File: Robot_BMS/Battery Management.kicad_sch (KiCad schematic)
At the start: 13 parts, among them IC1 BQ76922RSNR

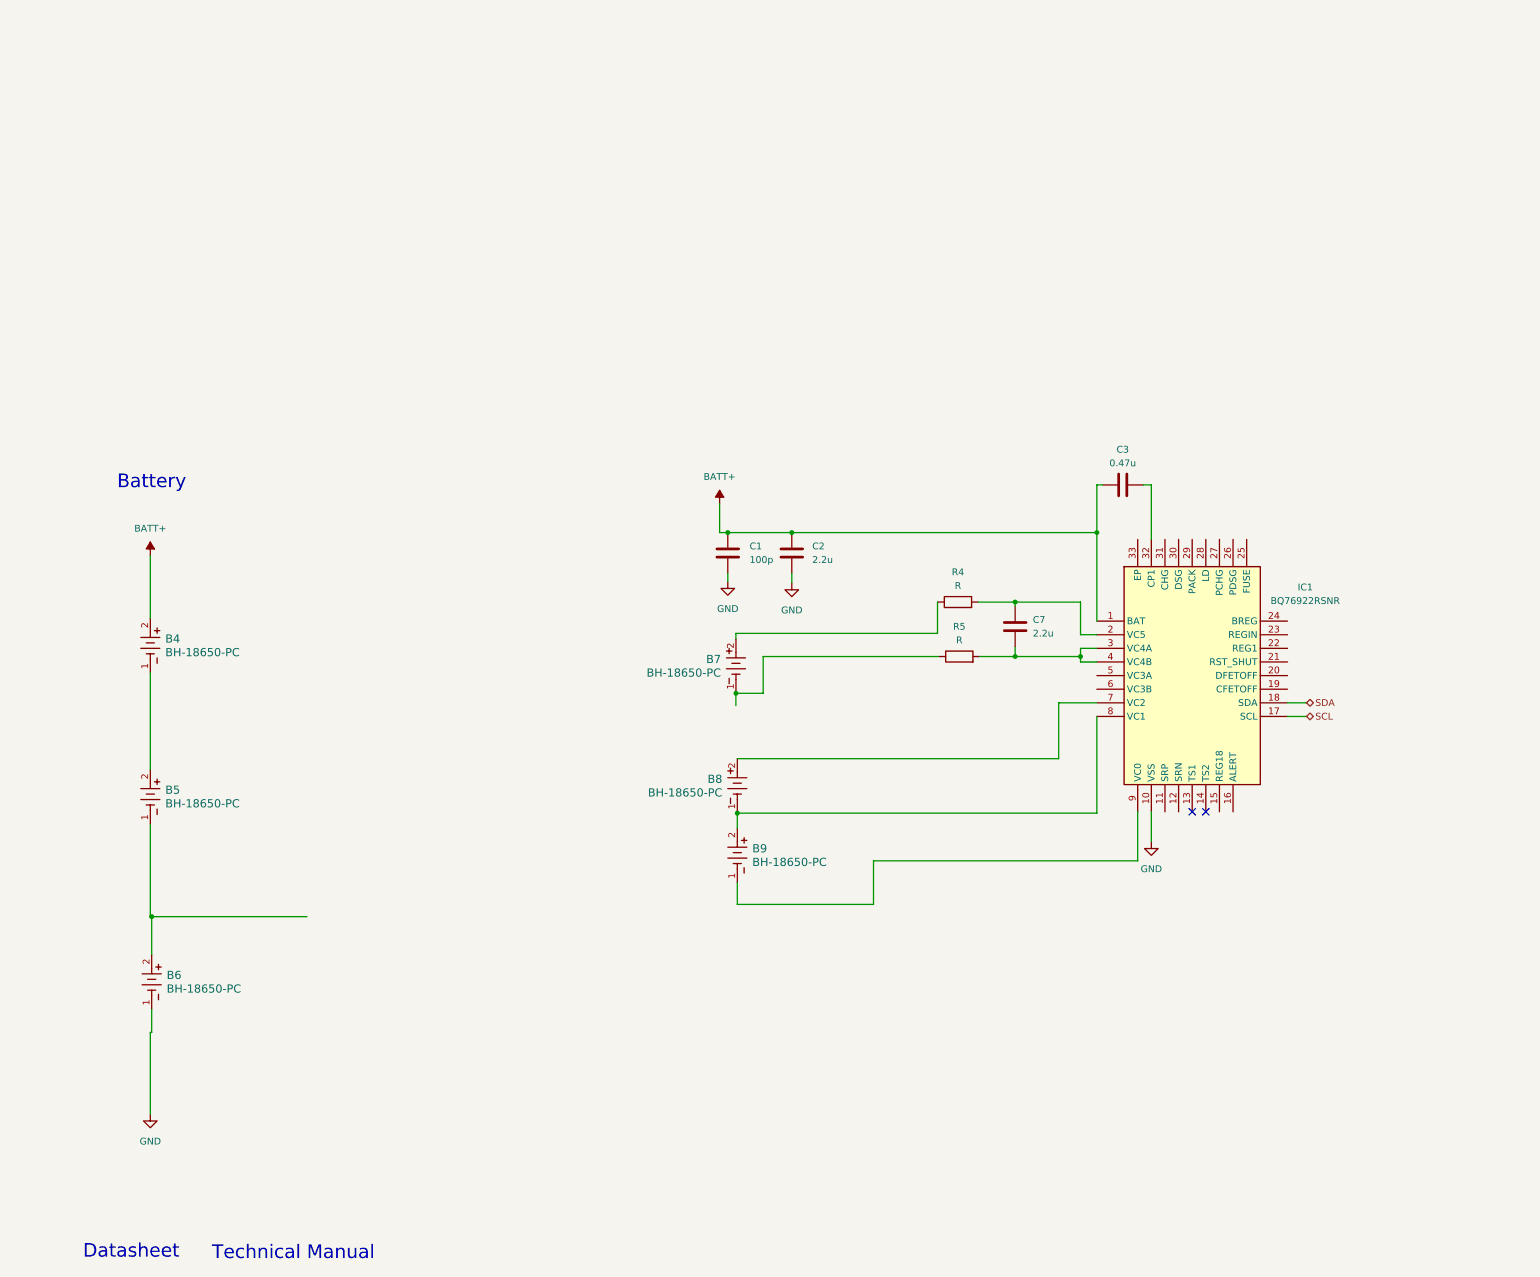
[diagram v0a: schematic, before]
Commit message: System drawing down on top schematic, will start inputting footprints
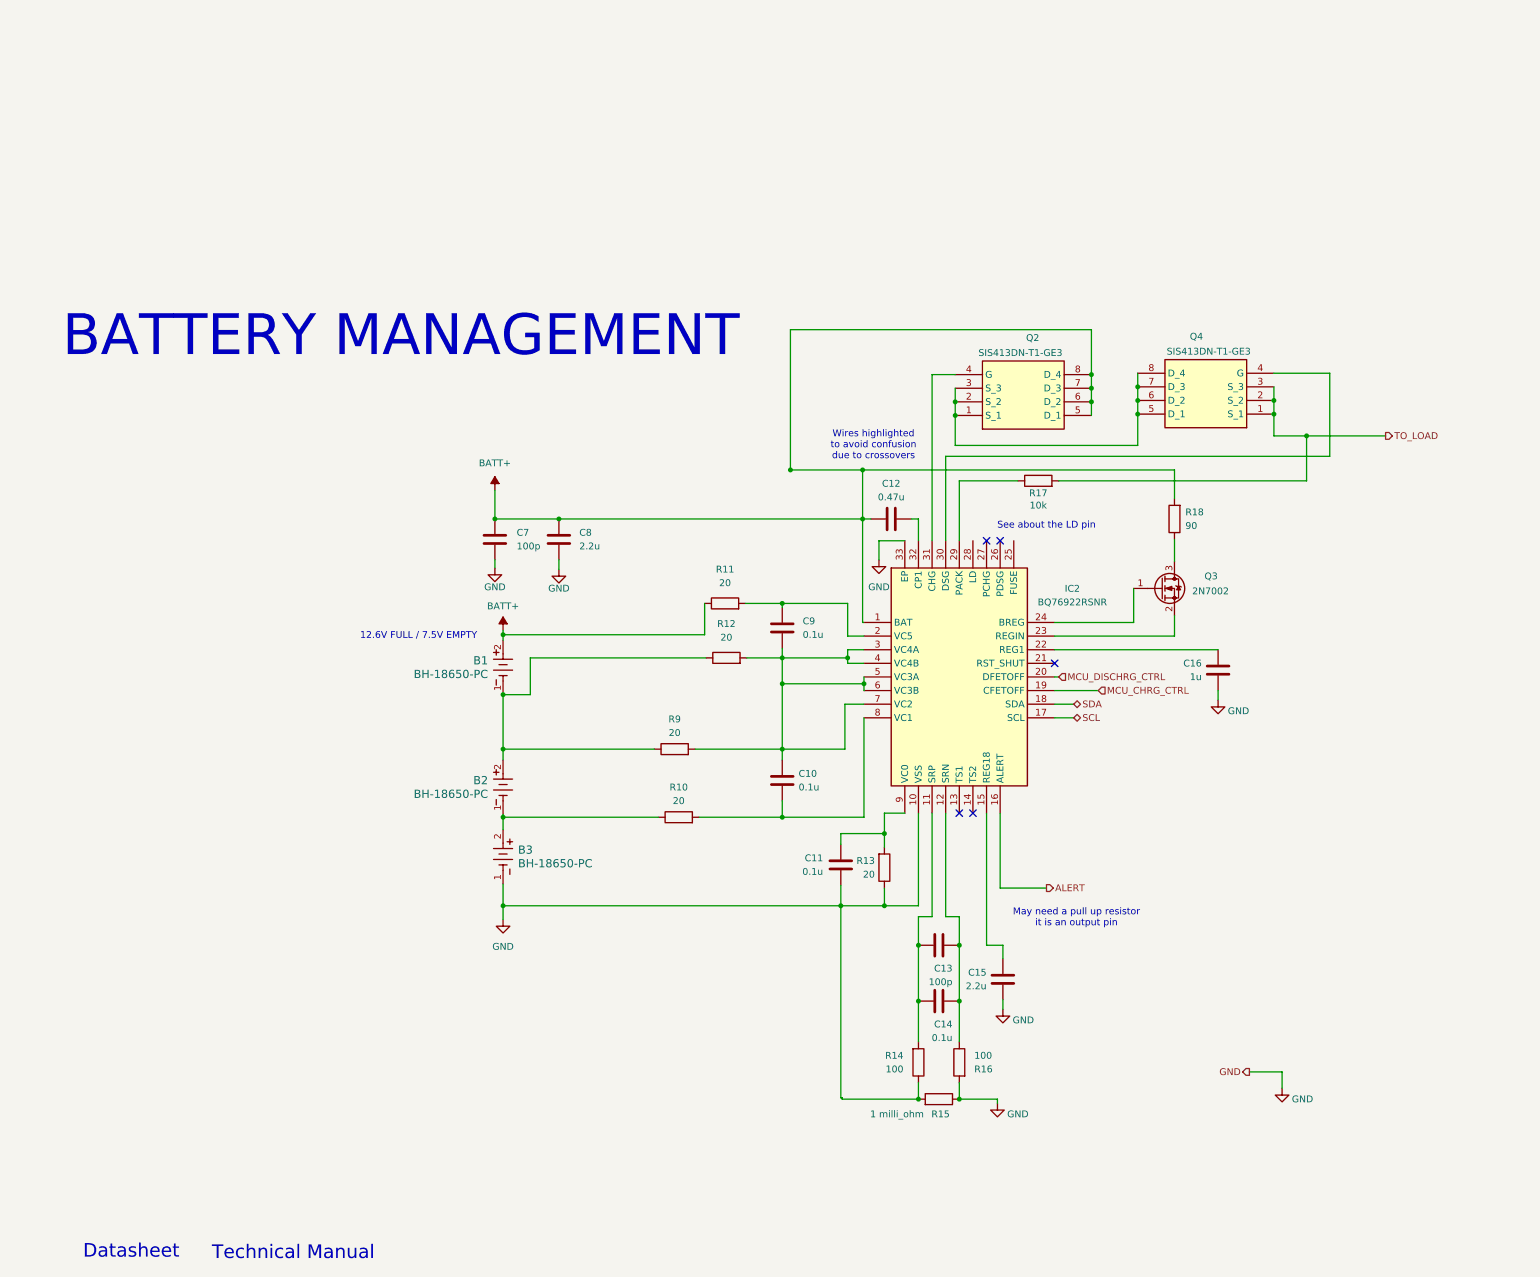
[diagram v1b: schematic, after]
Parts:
- removed B4, B5, B6: BH-18650-PC, BAT_BH-18650-PC_MPD, symbol 18650 Battery Holder:BH-18650-PC
- added C10, C11, C14: 0.1u, symbol Device:C
- added C13: 100p, symbol Device:C
- added C15: 2.2u, symbol Device:C
- added C16: 1u, symbol Device:C
- added Q2, Q4: SIS413DN-T1-GE3, SIS862DNT1GE3, symbol SIS413DN-T1-GE3:SIS413DN-T1-GE3
- added Q3: 2N7002, Package_TO_SOT_SMD:SOT-23, symbol Transistor_FET:2N7002
- added R10, R13, R9: 20, symbol Device:R
- added R14, R16: 100, symbol Device:R
- added R15: 1 milli_ohm, symbol Device:R
- added R17: 10k, symbol Device:R
- added R18: 90, symbol Device:R
- C9: renamed from C7; value 2.2u -> 0.1u
- R11: renamed from R4; value R -> 20
- R12: renamed from R5; value R -> 20
- renumbered B7 to B1, B8 to B2, B9 to B3, C3 to C12, C1 to C7, C2 to C8, IC1 to IC2
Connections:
- net BATT+: now also B1.2, R11.1, Q2.5 (D_1), Q2.6 (D_2), Q2.7 (D_3), Q2.8 (D_4), R18.2
- net GND: now also B3.1, IC2.33 (EP), C11.1, C15.1, C16.1, R13.1, R14.1, R15.1, R15.2, R16.2
- net at IC2.11 (SRP): now also C13.2, C14.2, R14.2
- net at IC2.12 (SRN): now also C13.1, C14.1, R16.1
- net at IC2.15 (REG18): now also C15.2
- net ALERT: now reaches IC2.16 (ALERT)
- net MCU_CHRG_CTRL: now reaches IC2.19 (CFETOFF)
- net MCU_DISCHRG_CTRL: now reaches IC2.20 (DFETOFF)
- net at IC2.22 (REG1): now also C16.2
- net at IC2.23 (REGIN): now also Q3.2 (S)
- net at IC2.24 (BREG): now also Q3.1 (G)
- net at IC2.29 (PACK): now also R17.1
- net at C9.1, IC2.3 (VC4A), IC2.4 (VC4B)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: now also IC2.5 (VC3A), IC2.6 (VC3B), IC2.7 (VC2), C10.2, R9.2
- net at IC2.30 (DSG): now also Q4.4 (G)
- net at IC2.31 (CHG): now also Q2.4 (G)
- net at B2.2: now also B1.1, R12.1, R9.1; no longer IC2.7 (VC2)
- net at B2.1, B3.2: now also R10.1; no longer IC2.8 (VC1)
- net at IC2.9 (VC0): now also C11.2, R13.2; no longer B3.1
- new net: C10.1, IC2.8 (VC1), R10.2
- new net: Q2.1 (S_1), Q2.2 (S_2), Q2.3 (S_3), Q4.5 (D_1), Q4.6 (D_2), Q4.7 (D_3), Q4.8 (D_4)
- new net: Q3.3 (D), R18.1
- new net TO_LOAD: Q4.1 (S_1), Q4.2 (S_2), Q4.3 (S_3), R17.2
- no-connect marks 2 -> 5
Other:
- note added: "12.6V FULL / 7.5V EMPTY"
- note added: "BATTERY MANAGEMENT"
- note added: "May need a pull up resistor it is an output pin"
- note added: "See about the LD pin"
- note added: "Wires highlighted to avoid confusion due to crossovers"
- note removed: "Battery"
- moved on the sheet: B1, B2, B3, C12, C7, C8, C9, IC2, R11, R12

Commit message: adding footprints and actual passive components
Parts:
- B1, B2, B3: footprint BAT_BH-18650-PC_MPD -> RobotBMS:BAT_BH-18650-PC_MPD
- IC2: footprint QFN40P400X400X80-33N-D -> RobotBMS:QFN40P400X400X80-33N-D
- Q2, Q4: footprint SIS862DNT1GE3 -> RobotBMS:SIS862DNT1GE3
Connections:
- no-connect marks 5 -> 7
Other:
- note added: "All standard Passive componenets are 0603 imperial"
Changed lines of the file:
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@@
 	)
 	(no_connect
+		(at 191.516 57.15)
+	)
+	(no_connect
 		(at 188.976 57.15)
 	)
@@
 	)
 	(no_connect
+		(at 183.896 57.15)
+	)
+	(no_connect
 		(at 181.356 107.95)
 	)
@@
 		)
 	)
+	(text "All standard Passive\ncomponenets are 0603 imperial"
+		(exclude_from_sim no)
+		(at 216.916 172.466 0)
+		(effects
+			(font
+				(size 2.54 2.54)
+			)
+		)
+	)
 	(hierarchical_label "GND"
 		(shape output)
@@
 			)
 		)
-		(property "Footprint" "QFN40P400X400X80-33N-D"
+		(property "Footprint" "RobotBMS:QFN40P400X400X80-33N-D"
 			(at 195.326 159.69 0)
 			(effects
@@
 			)
 		)
-		(property "Footprint" "SIS862DNT1GE3"
+		(property "Footprint" "RobotBMS:SIS862DNT1GE3"
 			(at 202.184 -61.138 0)
 			(effects
@@
 			)
 		)
-		(property "Footprint" "SIS862DNT1GE3"
+		(property "Footprint" "RobotBMS:SIS862DNT1GE3"
 			(at 218.44 -61.392 0)
 			(effects
@@
 			)
 		)
-		(property "Footprint" "BAT_BH-18650-PC_MPD"
+		(property "Footprint" "RobotBMS:BAT_BH-18650-PC_MPD"
 			(at 96.266 98.044 0)
 			(effects
@@
 			)
 		)
-		(property "Footprint" "BAT_BH-18650-PC_MPD"
+		(property "Footprint" "RobotBMS:BAT_BH-18650-PC_MPD"
 			(at 96.266 75.692 0)
 			(effects
@@
 			)
 		)
-		(property "Footprint" "BAT_BH-18650-PC_MPD"
+		(property "Footprint" "RobotBMS:BAT_BH-18650-PC_MPD"
 			(at 96.266 110.998 0)
 			(effects

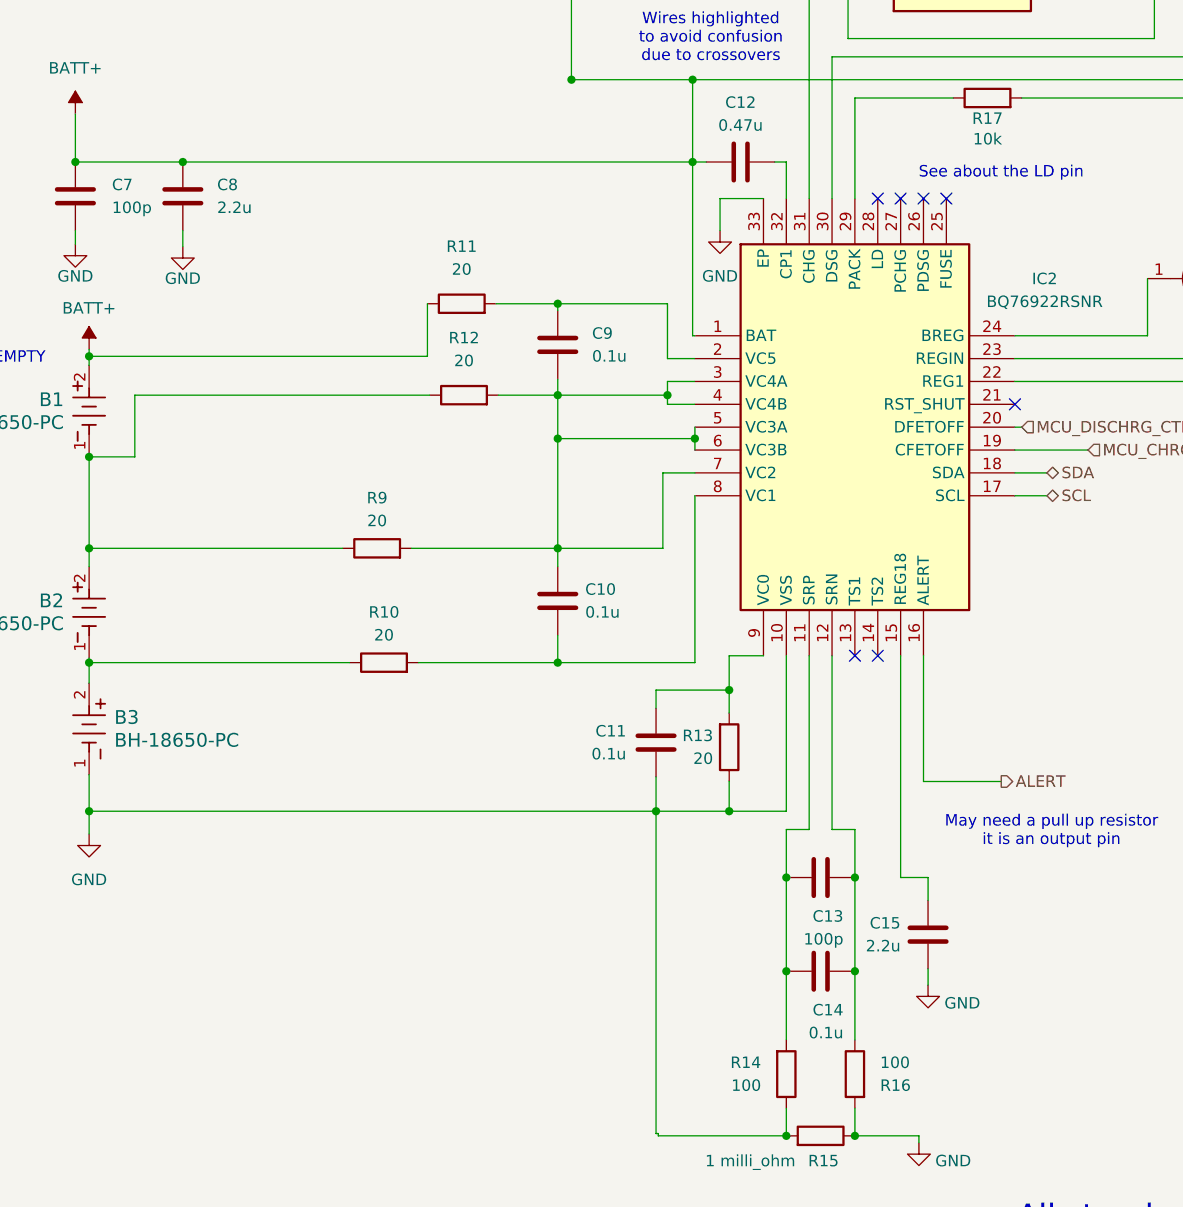
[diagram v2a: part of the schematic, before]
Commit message: adding footprints and actual passive components pt.2
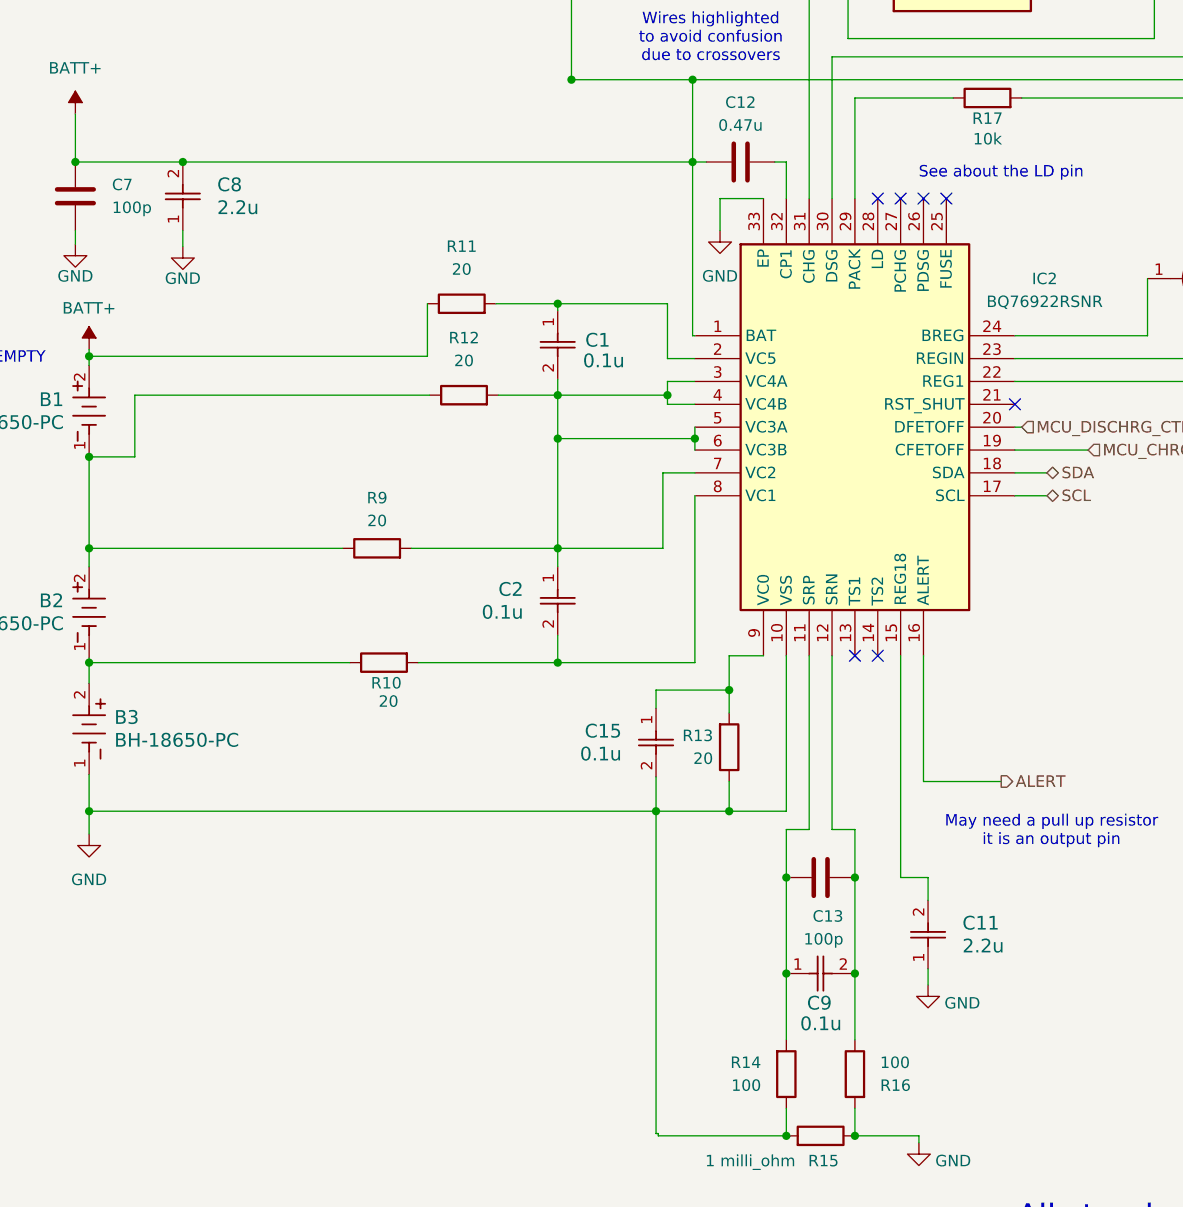
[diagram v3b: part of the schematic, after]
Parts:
- removed C10, C11, C14, C9: 0.1u, symbol Device:C
- removed C15, C8: 2.2u, symbol Device:C
- added C1, C15, C2, C9: 0.1u, CAPC17595_87N_KEM, symbol C0603C104K5RACAUTO:C0603C104K5RACAUTO
- added C11, C8: 2.2u, RobotBMS:CAP_GRM188R61H225KE11__MUR, symbol GRM188R61H225KE11D:GRM188R61H225KE11D
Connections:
- net BATT+: now also C8.2
- net GND: now also C11.1, C15.2, C8.1
- net at C13.1, IC2.12 (SRN), R16.1: now also C9.2
- net at C13.2, IC2.11 (SRP), R14.2: now also C9.1
- net at IC2.15 (REG18): now also C11.2
- net at IC2.2 (VC5), R11.2: now also C1.1
- net at IC2.3 (VC4A), IC2.4 (VC4B), IC2.5 (VC3A)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: now also C1.2, C2.1
- net at IC2.8 (VC1), R10.2: now also C2.2
- net at IC2.9 (VC0), R13.2: now also C15.1
